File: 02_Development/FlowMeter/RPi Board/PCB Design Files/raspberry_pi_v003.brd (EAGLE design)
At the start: 111.8 x 128.3 mm, 113 parts, among them J5 POWER_JACK, P1 SPL006-007, P2 SPL006-007, P3 SPL006-007, P4 SPL006-007, P5 SPL006-007, Q2 500mA/300V, U6 TCA9548APWR, U7 TCA9548APWR

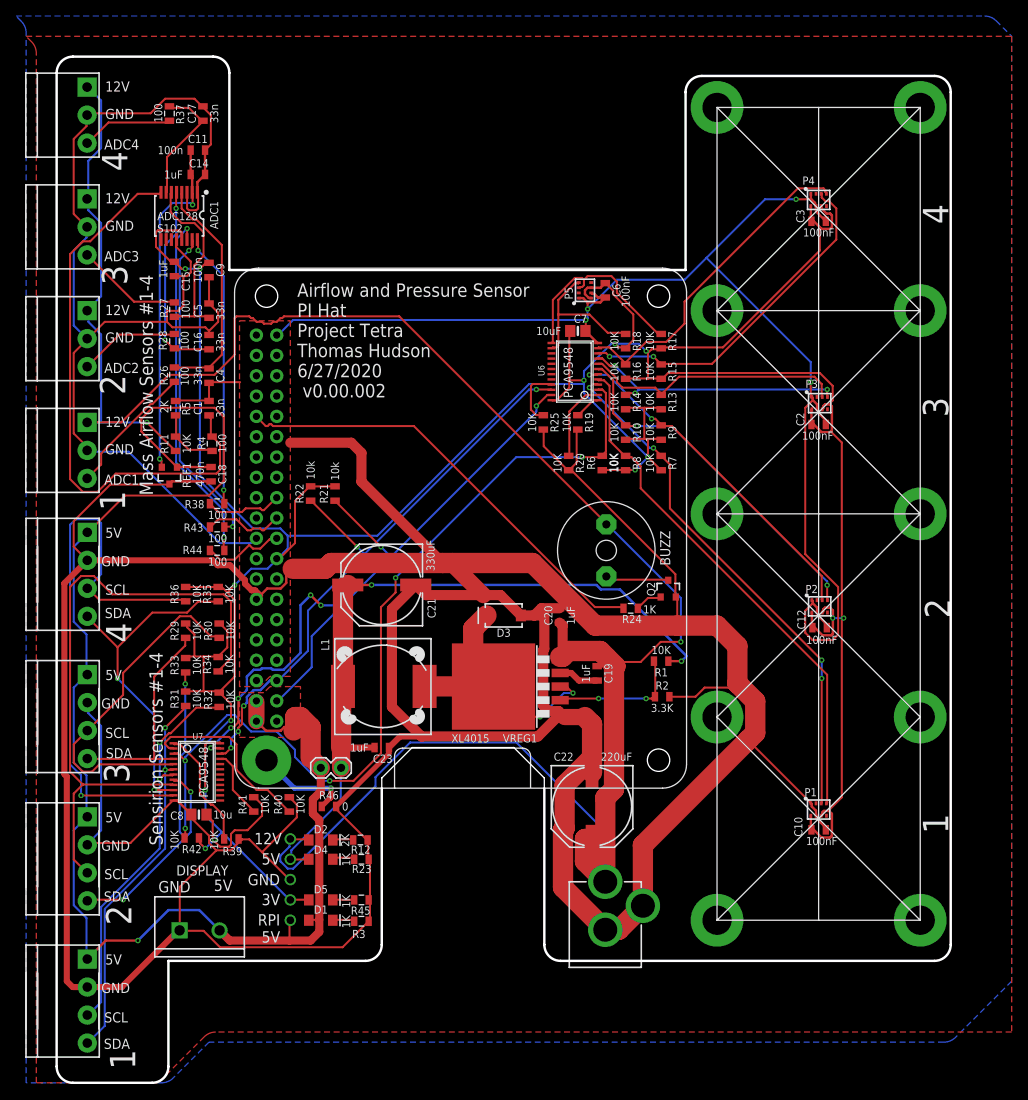
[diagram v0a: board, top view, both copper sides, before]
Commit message: add new PCB v003 with updates (#135)
- added hard reset for sensirion using p-channel moseft
- added capacior per the updated cut sheet v1.6 for the 5V regulator
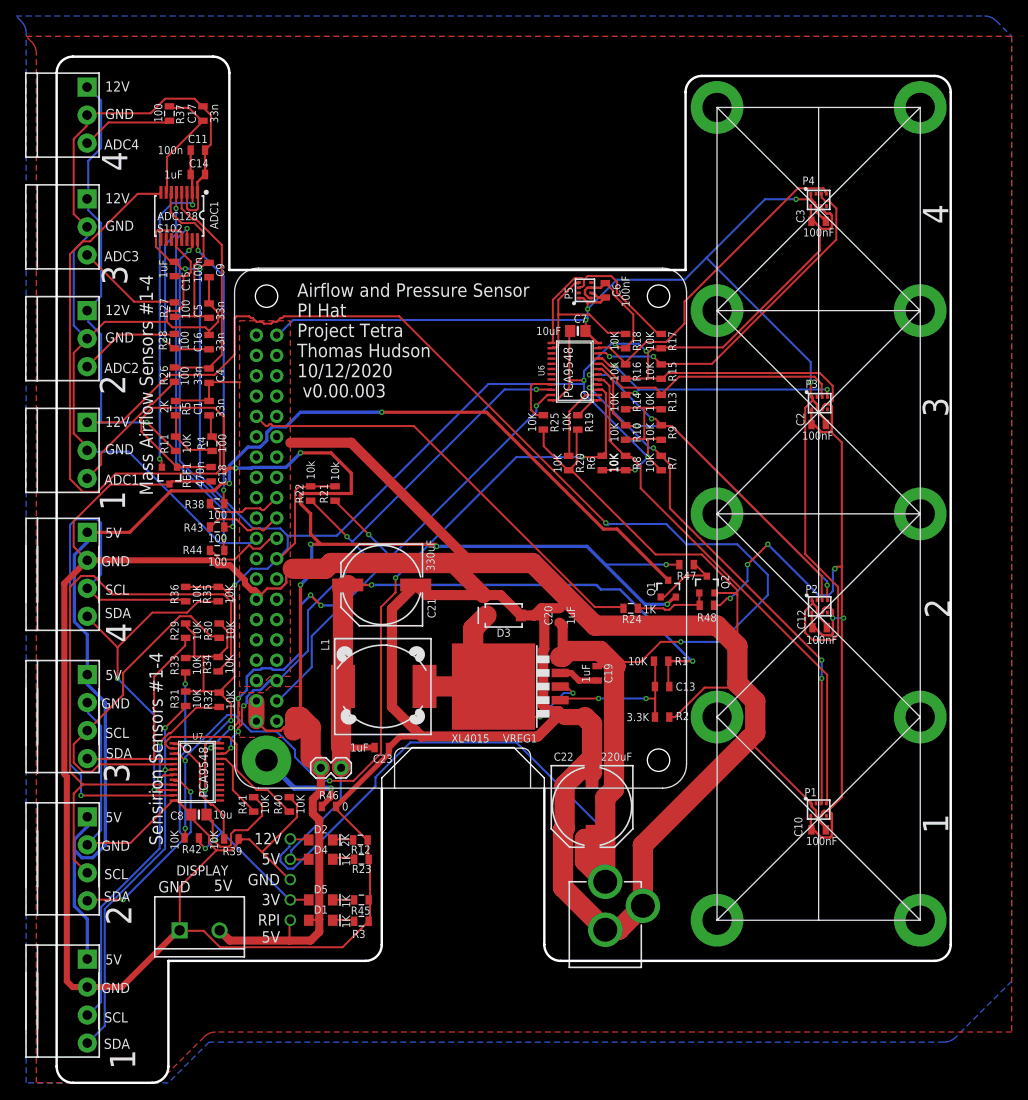
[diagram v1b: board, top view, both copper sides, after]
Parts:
- removed SP2: AL60P, buzzer:AL60P
- added C13: 33n, SparkFun-Capacitors:0805
- added Q1: 4.3A/20V/54mΩ, SparkFun-DiscreteSemi:SOT23-3
- added R47, R48: 10K, SparkFun-Resistors:0805
- moved Q2 4.85 mm to (50.8, -8.89)
- moved R2 2.54 mm to (45.2, -25.4)
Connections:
- new net SENS_POWER: J3.1, J7.1, J8.1, J9.1, Q1.3
- net 12V: no longer SP2.1
- net 3.3V: now also R48.1
- net 5V: now also C13.1
- net N$10: now also R48.2
- net N$11: now also C13.2
- net N$9: now also Q1.1, R47.1; no longer SP2.2
- net PI_5V_POWER: now also Q1.2, R47.2; no longer J3.1, J7.1, J8.1, J9.1
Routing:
- net SENS_POWER: track 0.00 -> 154.8 mm, vias 0 -> 2
- net 3.3V: track 454.9 -> 481.6 mm, vias 14 -> 18
- net 12V: track 284.8 -> 304.9 mm, vias 2 -> 3
- net PI_5V_POWER: track 185.5 -> 202.1 mm, vias 1 -> 7
- net GND: track 886.1 -> 900.3 mm
- net N$10: track 3.43 -> 9.56 mm
- net N$11: track 16.7 -> 21.5 mm
- net 5V: track 94.0 -> 97.9 mm
- net N$9: track 7.96 -> 9.04 mm
- net N$6: track 35.7 -> 34.7 mm
- net SCL: track 75.3 -> 76.2 mm
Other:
- board text added: "Airflow and Pressure Sensor PI Hat Project Tetra Thomas Hudson 10/12/2020 v0.00.003"
- board text removed: "Airflow and Pressure Sensor PI Hat Project Tetra Thomas Hudson 6/27/2020 v0.00.002"
- board text removed: "BUZZ"
